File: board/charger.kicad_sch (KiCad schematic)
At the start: 11 parts, among them U901 BQ24259RGE

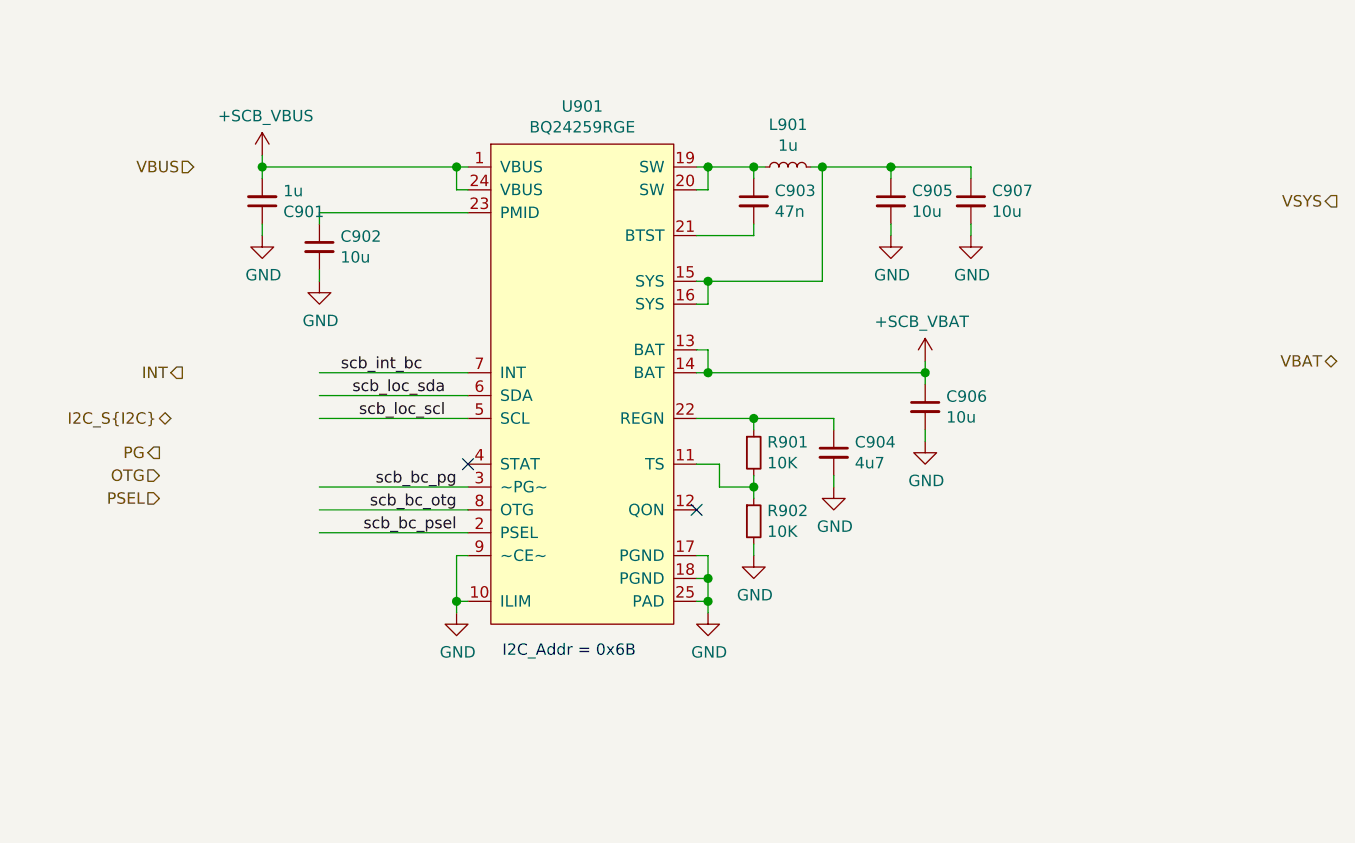
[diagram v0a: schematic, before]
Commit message: Added testpoints and other fixes
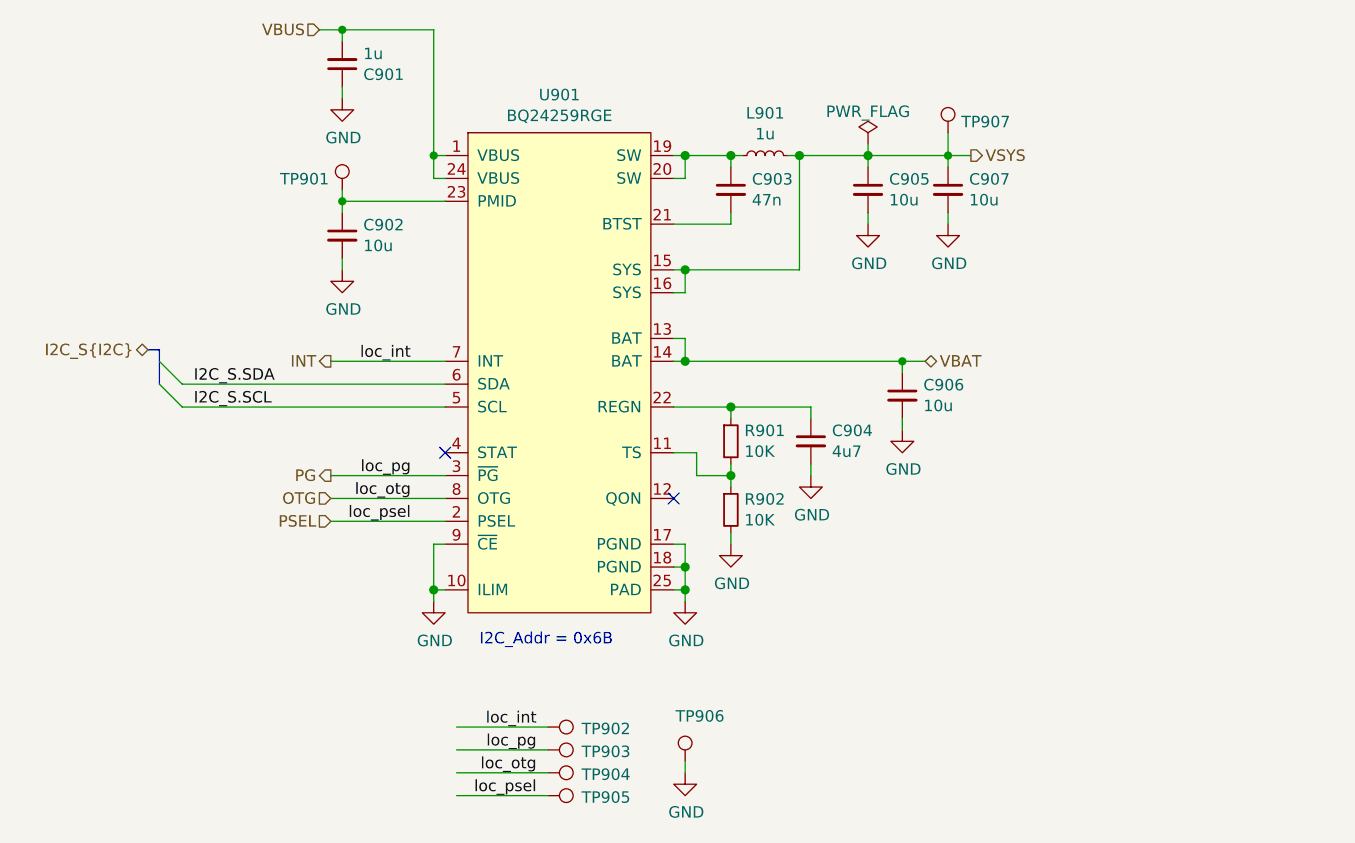
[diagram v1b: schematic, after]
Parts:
- added TP901, TP902, TP903, TP904, TP905, TP906, TP907: TestPoint, DIYPie:TestPoint_Pad_D1.5mm, symbol DIYPie:TestPoint
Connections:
- net scb_bc_otg is gone; now on net OTG: U901.8 (OTG)
- net scb_bc_pg is gone; now on net PG: U901.3 (~{PG})
- net scb_bc_psel is gone; now on net PSEL: U901.2 (PSEL)
- net scb_int_bc is gone; now on net INT: U901.7 (INT)
- net GND: now also TP906.1
- net INT: now also TP902.1
- net OTG: now also TP904.1
- net PG: now also TP903.1
- net PSEL: now also TP905.1
- net VBAT: now also C906.1, U901.13 (BAT), U901.14 (BAT)
- net VBUS: now also C901.2, U901.1 (VBUS), U901.24 (VBUS)
- net VSYS: now also C905.1, C907.1, L901.2, U901.15 (SYS), U901.16 (SYS), TP907.1
- net at C902.1, U901.23 (PMID): now also TP901.1
- removed net +5V: C901.2, C906.1, U901.1 (VBUS), U901.13 (BAT), U901.14 (BAT), U901.24 (VBUS)
- net scb_loc_scl renamed I2C_S.SCL
- net scb_loc_sda renamed I2C_S.SDA
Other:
- moved on the sheet: C901, C902, C903, C904, C905, C906, C907, L901, R901, R902, U901
